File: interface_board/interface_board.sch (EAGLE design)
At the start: 101 parts, among them IC1 V7805-1000, IC6 LAN9512-JZX, K1 61400416021, Q6 CTS_32X25_SMD, U1 SFW15R-1STE1LF, U2 SFW15R-1STE1LF, U3 DMG1012T, U5 PAM2306DYPAA

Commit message: picam360
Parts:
- removed C11: UUD1A220MCL1GS(22u), resistor:CPOL-EU153CLV-0405
- removed C15: UUD1E100MCL1GS(10u), resistor:CPOL-EU153CLV-0405
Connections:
- removed net 3V3A1: C32.2, C33.2, C34.2, C35.2, C36.2, C37.2, C38.2, FB2.P$1, IC6.VDD33A@1, IC6.VDD33A@2, IC6.VDD33A@3, IC6.VDD33A@4, IC6.VDD33A@5, IC6.VDD33A@6, IC6.VDD33A@7
- removed net N$47: IC6.USBDM2, JP5.D-
- removed net N$48: IC6.USBDP2, JP5.D+
- removed net USBD3_N: IC6.USBDM3, K1.D-
- removed net USBD3_P: IC6.USBDP3, K1.D+
- new net USB3_N: IC6.USBDM3, JP5.D-
- new net USB3_P: IC6.USBDP3, JP5.D+
- new net USBD2_N: IC6.USBDM2, K1.D-
- new net USBD2_P: IC6.USBDP2, K1.D+
- net +5V: no longer C11.+
- net 3V3A: now also C32.2, C33.2, C34.2, C35.2, C36.2, C37.2, C38.2, FB2.P$1, IC6.VDD33A@1, IC6.VDD33A@2, IC6.VDD33A@3, IC6.VDD33A@4, IC6.VDD33A@5, IC6.VDD33A@6, IC6.VDD33A@7
- net GND: no longer C11.-, C15.-
- net N$39: no longer C15.+

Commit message: interface board
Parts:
- removed C16: 1u, resistor:C-EUC0402
- removed C17: 10n, resistor:C-EUC0402
- removed F1: MF-MSMF200-2, openblw:MF-MSMF075/24
- removed FB1, FB4: HR2220V801R-10, resistor:L-EUL5650M
- removed IC1: V7805-1000, openblw:VR_1OUTXX
- removed JP2, JP3: M20-9980346, pinhead:PINHD-2X3
- removed JP4: M20-9990246, openblw:PINHD-1X2
- removed L3: SRP1245A-100M, openblw:SRP1250A
- removed R18: 1K, resistor:R-EU_R0402
- removed U$1: 282836-2, openblw:282836-2
- removed U$2: M20-9980346, openblw:282836-2
- JP1: device pinhead:PINHD-2X4 -> pinhead:PINHD-2X20
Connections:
- removed net +12V: C16.1, F1.1, L3.2, U$2.CON01
- removed net AGND: FB4.1, JP2.5, JP2.6, U$1.CON01
- removed net AVCC: FB1.1, JP2.1, JP2.2, U$1.CON02
- removed net N$38: C17.1, R18.2
- removed net N$39: F1.2, IC1.IN
- removed net N$6: FB1.2, L3.1, R18.1
- net +3V3: no longer JP3.5, JP3.6, JP4.1
- net +5V: no longer IC1.OUT
- net GND: now also JP1.13, JP1.14; no longer C16.2, C17.2, FB4.2, IC1.GND, JP3.1, JP4.2, U$2.CON02

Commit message: refactoring
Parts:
- removed C12, C13, C14: 47u, resistor:C-EUC1206
- removed C4, C5: 100p, resistor:C-EUC0402
- removed C6, C7: 10u, resistor:C-EUC0805
- removed L1, L2: SRN4018-4R7M(4.7u), openblw:BOURNS-SRN4018
- removed PCB1: 1473005-4, openblw:RPI_COMPUTE
- removed R11, R12, R4, R5: 100K, resistor:R-EU_R0402
- removed R13, R14, R16, R17: 1.8K, resistor:R-EU_R0402
- removed R15, R6: 470R, resistor:R-EU_R0402
- removed R7, R8, R9: 0R, resistor:R-EU_R0805
- removed U3: DMG1012T, openblw:DMG1012T
- removed U5: PAM2306DYPAA, openblw:PAM2306
- added C16: 1u, resistor:C-EUC0402
- added C17: 10n, resistor:C-EUC0402
- added FB1, FB4: HR2220V801R-10, resistor:L-EUL5650M
- added IC1: V7805-1000, openblw:VR_1OUTXX
- added JP2, JP3: M20-9980346, pinhead+:PINHD-2X3SMT
- added JP4: (no value), pinhead:PINHD-1X3
- added L3: SRP1245A-100M, openblw:SRP1250A
- added Q1: IRLML6346TRPBF, openblw:NMOS-FETSOT23
- added R18: 1K, resistor:R-EU_R0402
- added U$2, U$4, U$7, U$8: 282836-2, openblw:282836-2
- C10, C41, C42: device rcl:C-EUC0805 -> resistor:C-EUC0402
- C2: value 10u -> UWT1E221MNL1GS(220u); device resistor:C-EUC0805 -> resistor:CPOL-EU153CLV-0810
- C21, C22, C23, C24, C26, C27, C28, C29, C30, C31, C32, C33, C34, C35, C36, C37, C38, C39, C40, C43, C44, C45, C8, C9: device rcl:C-EUC0603 -> resistor:C-EUC0402
- C3: value 10u -> 1uF; device resistor:C-EUC0805 -> SparkFun-Capacitors:CAP0603-CAP
- JP1: value M20-9980446 -> M20-9990446; device pinhead:PINHD-2X20 -> pinhead:PINHD-2X5
- JP5: value USB-IDMICRO -> (none); device openblw:USB-IDMICRO -> pinhead:PINHD-1X3
- LED1: value RED -> LTW-5630AZL50; device led:LEDCHIP-LED0603 -> openblw:LTW-5630AZL
- LED2: value GREEN -> LTW-5630AZL50; device led:LEDCHIP-LED0603 -> openblw:LTW-5630AZL
- R1: value 100K -> 4.99K
- R10, R19, R20, R25, R26, R27, R28, R29, R30, R31, R32, R33: device rcl:R-EU_R0603 -> resistor:R-EU_R0402
- R2: value 450K -> 100K
- R3: value 200K -> 1K
- U1: value SFW15R-1STE1LF -> AL5812MP-13; device openblw:RPI_CAMERA -> openblw:AL5812MP-13
- U2: value SFW15R-1STE1LF -> MPU-9250; device openblw:RPI_CAMERA -> invensense:MPU-9250
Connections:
- removed net +1V8: C5.1, C7.1, L2.1, R3.1, R9.2
- removed net BOTTOM_LIGHT_ENABLED: PCB1.59/GPIO17
- removed net CAM0_C_N: PCB1.144/CAM0_CN*, U1.CAM_CK_N@8
- removed net CAM0_C_P: PCB1.142/CAM0_CP*, U1.CAM_CK_P@9
- removed net CAM0_D0_N: PCB1.138/CAM0_DN0*, U1.CAM_D0_N@2
- removed net CAM0_D0_P: PCB1.136/CAM0_DP0*, U1.CAM_D0_P@3
- removed net CAM0_D1_N: PCB1.150/CAM0_DN1*, U1.CAM_D1_N@5
- removed net CAM0_D1_P: PCB1.148/CAM0_DP1*, U1.CAM_D1_P@6
- removed net CAM0_IO0: PCB1.36/GPIO31, U1.CAM_IO0@11
- removed net CAM0_IO1: PCB1.34/GPIO30, U1.CAM_IO1@12
- removed net CAM0_SCL: PCB1.30/GPIO29, R13.1, U1.CAM_SCL@13
- removed net CAM0_SDA: PCB1.28/GPIO28, R14.1, U1.CAM_SDA@14
- removed net CAM1_C_N: PCB1.149/CAM1_CN*, U2.CAM_CK_N@8
- removed net CAM1_C_P: PCB1.147/CAM1_CP*, U2.CAM_CK_P@9
- removed net CAM1_D0_N: PCB1.161/CAM1_DN0*, U2.CAM_D0_N@2
- removed net CAM1_D0_P: PCB1.159/CAM1_DP0*, U2.CAM_D0_P@3
- removed net CAM1_D1_N: PCB1.155/CAM1_DN1*, U2.CAM_D1_N@5
- removed net CAM1_D1_P: PCB1.153/CAM1_DP1*, U2.CAM_D1_P@6
- removed net CAM1_IO0: PCB1.11/GPIO3, U2.CAM_IO0@11
- removed net CAM1_IO1: PCB1.9/GPIO2, U2.CAM_IO1@12
- removed net CAM1_SCL: PCB1.5/GPIO1, R17.1, U2.CAM_SCL@13
- removed net CAM1_SDA: PCB1.3/GPIO0, R16.1, U2.CAM_SDA@14
- removed net CM_1V8: C12.1, PCB1.183/1V8, PCB1.184/1V8, PCB1.185/1V8, PCB1.186/1V8, R9.1
- removed net CM_3V3: C13.1, PCB1.189/VDAC, PCB1.190/VDAC, PCB1.191/3V3, PCB1.192/3V3, PCB1.193/3V3, PCB1.194/3V3, R8.1
- removed net CM_VBAT: C14.1, PCB1.197/VBAT, PCB1.198/VBAT, PCB1.199/VBAT, PCB1.200/VBAT, R7.1
- removed net EMMC_DISABLE_N: PCB1.2/EMMC_DISABLE_N
- removed net EXT0/UART1_TX: JP1.6, PCB1.70/GPIO40
- removed net EXT1/UART1_RX: JP1.4, PCB1.72/GPIO41
- removed net GPIO47_1V8: PCB1.90/GPIO47_1V8, U3.G
- removed net N$10: C5.2, R3.2, R4.1, U5.FB2@10
- removed net N$11: PCB1.154/NC
- removed net N$12: PCB1.156/NC
- removed net N$13: PCB1.158/NC
- removed net N$14: PCB1.160/NC
- removed net N$15: PCB1.162/NC
- removed net N$16: PCB1.10/NC
- removed net N$17: PCB1.12/NC
- removed net N$18: PCB1.14/NC
- removed net N$19: PCB1.16/NC
- removed net N$2: L1.2, U5.LX1@8
- removed net N$20: PCB1.18/NC
- removed net N$21: PCB1.20/NC
- removed net N$22: PCB1.22/NC
- removed net N$23: PCB1.24/NC
- removed net N$24: PCB1.124/NC
- removed net N$25: PCB1.126/NC
- removed net N$26: PCB1.128/NC
- removed net N$27: PCB1.130/NC
- removed net N$28: PCB1.132/NC
- removed net N$29: PCB1.4/NC
- removed net N$30: PCB1.6/NC
- removed net N$31: PCB1.82/GPIO44, R12.1
- removed net N$32: LED2.A, R15.2
- removed net N$33: LED2.C, U3.D
- removed net N$34: PCB1.84/GPIO45, R11.1
- removed net N$35: PCB1.8/NC
- removed net N$8: C4.2, R2.2, R5.1, U5.FB1@4
- removed net TOP_LIGHT_ENABLED: PCB1.57/GPIO16
- removed net UART0_RX: JP1.5, PCB1.53/GPIO15
- removed net UART0_TX: JP1.3, PCB1.51/GPIO14
- removed net USB3_N: IC6.USBDM3, JP5.D-
- removed net USB3_P: IC6.USBDP3, JP5.D+
- new net +12V: C1.2, C16.1, C2.+, IC1.IN, L3.2, LED1.A, U$4.CON02, U1.VCC
- new net AGND: FB4.1, JP2.5, JP2.6, U$2.CON02
- new net AIN1: JP1.6
- new net AIN2: JP1.5
- new net AOUT1: U$8.CON01
- new net AOUT2: U$8.CON02
- new net AVCC: FB1.1, JP2.1, JP2.2, U$2.CON01
- new net BIN1: JP1.7
- new net BIN2: JP1.8
- new net BOUT1: U$7.CON02
- new net BOUT2: U$7.CON01
- new net LIGHT_PWM: JP1.1, R3.2
- new net N$38: C17.1, R18.2
- new net N$5: R1.2, U1.RSET
- new net N$6: Q1.D, R1.1
- new net PWMA: JP1.4
- new net PWMB: JP1.9
- new net TWI_SCL: U2.SCL/SCLK
- new net TWI_SDA: U2.SDA/SDI
- new net VCC: U2.NCS, U2.RESV, U2.VDD, U2.VDDIO
- net +3V3: now also JP1.2, JP3.5, JP3.6; no longer C4.1, C6.1, L1.1, PCB1.39/GPIO0-27_VREF, PCB1.40/GPIO0-27_VREF, PCB1.41/GPIO28-45_VREF, PCB1.42/GPIO28-45_VREF, R13.2, R14.2, R15.1, R16.2, R17.2, R2.1, R6.1, R7.2, R8.2, U1.CAM_3V3@15, U2.CAM_3V3@15
- net +5V: now also IC1.OUT; no longer C2.1, C3.1, JP1.1, JP1.2, JP5.VBUS, R1.1, U5.EN1@6, U5.VIN1@7, U5.VIN2@1
- net GND: now also C1.1, C16.2, C17.2, C2.-, C3.1, FB4.2, IC1.GND, JP1.10, JP1.3, JP3.1, Q1.S, R2.1, U$4.CON01, U1.EP, U1.GND, U2.ADO/SDO, U2.FSYNC, U2.GND, U2.RESV2; no longer C1.2, C12.2, C13.2, C14.2, C2.2, C3.2, C6.2, C7.2, JP1.13, JP1.14, JP1.7, JP1.8, JP5.GND, LED1.C, PCB1.1/GND, PCB1.103/GND, PCB1.104/GND, PCB1.109/GND, PCB1.110/GND, PCB1.115/GND, PCB1.121/GND, PCB1.122/GND, PCB1.127/GND, PCB1.13/GND, PCB1.133/GND, PCB1.134/GND, PCB1.139/GND, PCB1.140/GND, PCB1.145/GND, PCB1.146/GND, PCB1.151/GND, PCB1.152/GND, PCB1.157/GND, PCB1.163/GND, PCB1.164/GND, PCB1.168/USB_OTGID, PCB1.169/GND, PCB1.170/GND, PCB1.181/GND, PCB1.182/GND, PCB1.187/GND, PCB1.188/GND, PCB1.19/GND, PCB1.195/GND, PCB1.196/GND, PCB1.25/GND, PCB1.26/GND, PCB1.31/GND, PCB1.32/GND, PCB1.37/GND, PCB1.38/GND, PCB1.43/GND, PCB1.44/GND, PCB1.49/GND, PCB1.50/GND, PCB1.55/GND, PCB1.56/GND, PCB1.61/GND, PCB1.62/GND, PCB1.67/GND, PCB1.68/GND, PCB1.7/GND, PCB1.73/GND, PCB1.74/GND, PCB1.79/GND, PCB1.80/GND, PCB1.85/GND, PCB1.86/GND, PCB1.91/GND, PCB1.92/GND, PCB1.97/GND, PCB1.98/GND, R11.2, R12.2, R4.2, R5.2, U1.CAM_GND@1, U1.CAM_GND@10, U1.CAM_GND@4, U1.CAM_GND@7, U2.CAM_GND@1, U2.CAM_GND@10, U2.CAM_GND@4, U2.CAM_GND@7, U3.S, U5.GND@3, U5.GND@9, U5.PAD
- net LAN_RUN: no longer PCB1.21/GPIO6
- net N$1: now also LED1.C, LED2.A; no longer C1.1, R1.2, U5.EN2@12
- net N$3: now also FB1.2, L3.1, R18.1; no longer U5.NC1@5
- net N$4: now also C3.2, U2.REGOUT; no longer U5.NC2@11
- net N$7: now also Q1.G, R2.2, R3.1; no longer L2.2, U5.LX2@2
- net N$9: now also LED2.C, U1.LED; no longer LED1.A, R6.2
- net USB_D_N: no longer PCB1.167/USB_DM**
- net USB_D_P: no longer PCB1.165/USB_DP**
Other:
- note removed: "Camera"
- note removed: "Interfaces"
- note removed: "Power"
- note removed: "RPCM"

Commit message: refactoring
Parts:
- removed JP5: (no value), pinhead:PINHD-1X3
- added JP6: USB-IDMICRO, openblw:USB-IDMICRO
- JP2, JP3: device pinhead+:PINHD-2X3SMT -> pinhead:PINHD-2X3
- JP4: device pinhead:PINHD-1X3 -> pinhead:PINHD-2X3
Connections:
- net +5V: now also JP6.VBUS
- net GND: now also JP6.GND
- net USB_D_N: now also JP6.D-
- net USB_D_P: now also JP6.D+
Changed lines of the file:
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@@
 <part name="L3" library="openblw" deviceset="SRP1250A" device="" value="SRP1245A-100M"/>
 <part name="FB4" library="resistor" deviceset="L-EU" device="L5650M" value="HR2220V801R-10"/>
-<part name="JP2" library="pinhead+" deviceset="PINHD-2X3" device="SMT" value="M20-9980346"/>
-<part name="JP3" library="pinhead+" deviceset="PINHD-2X3" device="SMT" value="M20-9980346"/>
+<part name="JP2" library="pinhead" deviceset="PINHD-2X3" device="" value="M20-9980346"/>
+<part name="JP3" library="pinhead" deviceset="PINHD-2X3" device="" value="M20-9980346"/>
 <part name="V7" library="supply" deviceset="+3V3" device=""/>
 <part name="GND11" library="supply" deviceset="GND" device=""/>
@@
 <part name="Q6" library="raspi" deviceset="CTS_32X25_SMD" device=""/>
 <part name="GND53" library="supply1" deviceset="GND" device=""/>
-<part name="JP4" library="pinhead" deviceset="PINHD-1X3" device=""/>
-<part name="JP5" library="pinhead" deviceset="PINHD-1X3" device=""/>
 <part name="U2" library="invensense" deviceset="MPU-9250" device=""/>
 <part name="GND6" library="SparkFun-Aesthetics" deviceset="GND" device=""/>
 <part name="SUPPLY1" library="SparkFun-Aesthetics" deviceset="VCC" device=""/>
 <part name="C3" library="SparkFun-Capacitors" deviceset="CAP" device="0603-CAP" value="1uF"/>
+<part name="JP6" library="openblw" deviceset="USB-ID" device="MICRO"/>
+<part name="GND8" library="supply1" deviceset="GND" device=""/>
+<part name="P+1" library="supply1" deviceset="+5V" device=""/>
+<part name="JP4" library="pinhead" deviceset="PINHD-2X3" device=""/>
 </parts>
 <sheets>
@@
 <instance part="GND13" gate="1" x="332.74" y="137.16"/>
 <instance part="GND15" gate="1" x="304.8" y="137.16"/>
-<instance part="JP4" gate="A" x="116.84" y="142.24" rot="R180"/>
-<instance part="JP5" gate="A" x="116.84" y="132.08" rot="R180"/>
 <instance part="U2" gate="G$1" x="195.58" y="132.08"/>
 <instance part="GND6" gate="1" x="231.14" y="96.52"/>
 <instance part="SUPPLY1" gate="G$1" x="165.1" y="170.18"/>
 <instance part="C3" gate="G$1" x="167.64" y="124.46" rot="R90"/>
+<instance part="JP4" gate="A" x="101.6" y="129.54"/>
 </instances>
 <busses>
@@
 <instance part="Q6" gate="G$2" x="177.8" y="73.66" rot="R90"/>
 <instance part="GND53" gate="1" x="160.02" y="78.74" rot="R270"/>
+<instance part="JP6" gate="G$1" x="157.48" y="114.3" rot="R270"/>
+<instance part="GND8" gate="1" x="142.24" y="114.3"/>
+<instance part="P+1" gate="1" x="177.8" y="119.38" rot="R270"/>
 </instances>
 <busses>
@@
 <pinref part="GND53" gate="1" pin="GND"/>
 <junction x="162.56" y="78.74"/>
+</segment>
+<segment>
+<pinref part="JP6" gate="G$1" pin="GND"/>
+<wire x1="157.48" y1="116.84" x2="157.48" y2="119.38" width="0.1524" layer="91"/>
+<pinref part="GND8" gate="1" pin="GND"/>
+<wire x1="157.48" y1="119.38" x2="142.24" y2="119.38" width="0.1524" layer="91"/>
+<wire x1="142.24" y1="119.38" x2="142.24" y2="116.84" width="0.1524" layer="91"/>
 </segment>
 </net>
@@
 <pinref part="K1" gate="G$1" pin="VCC"/>
 </segment>
+<segment>
+<pinref part="JP6" gate="G$1" pin="VBUS"/>
+<wire x1="160.02" y1="116.84" x2="160.02" y2="119.38" width="0.1524" layer="91"/>
+<pinref part="P+1" gate="1" pin="+5V"/>
+<wire x1="160.02" y1="119.38" x2="175.26" y2="119.38" width="0.1524" layer="91"/>
+</segment>
 </net>
 <net name="USBD2_N" class="3">
@@
 <segment>
 <pinref part="IC6" gate="G$1" pin="USBDM0"/>
-<wire x1="238.76" y1="127" x2="177.8" y2="127" width="0.1524" layer="91"/>
-<label x="177.8" y="127" size="1.778" layer="95" rot="R180" xref="yes"/>
+<wire x1="238.76" y1="127" x2="162.56" y2="127" width="0.1524" layer="91"/>
+<label x="152.4" y="127" size="1.778" layer="95" rot="R180" xref="yes"/>
+<pinref part="JP6" gate="G$1" pin="D-"/>
+<wire x1="162.56" y1="127" x2="152.4" y2="127" width="0.1524" layer="91"/>
+<wire x1="162.56" y1="116.84" x2="162.56" y2="127" width="0.1524" layer="91"/>
+<junction x="162.56" y="127"/>
 </segment>
 </net>
@@
 <segment>
 <pinref part="IC6" gate="G$1" pin="USBDP0"/>
-<wire x1="238.76" y1="124.46" x2="177.8" y2="124.46" width="0.1524" layer="91"/>
-<label x="177.8" y="124.46" size="1.778" layer="95" rot="R180" xref="yes"/>
-</segment>
-</net>
+<wire x1="238.76" y1="124.46" x2="165.1" y2="124.46" width="0.1524" layer="91"/>
+<label x="152.4" y="124.46" size="1.778" layer="95" rot="R180" xref="yes"/>
+<pinref part="JP6" gate="G$1" pin="D+"/>
+<wire x1="165.1" y1="124.46" x2="152.4" y2="124.46" width="0.1524" layer="91"/>
+<wire x1="165.1" y1="116.84" x2="165.1" y2="124.46" width="0.1524" layer="91"/>
+<junction x="165.1" y="124.46"/>
+</segment>
+</net>

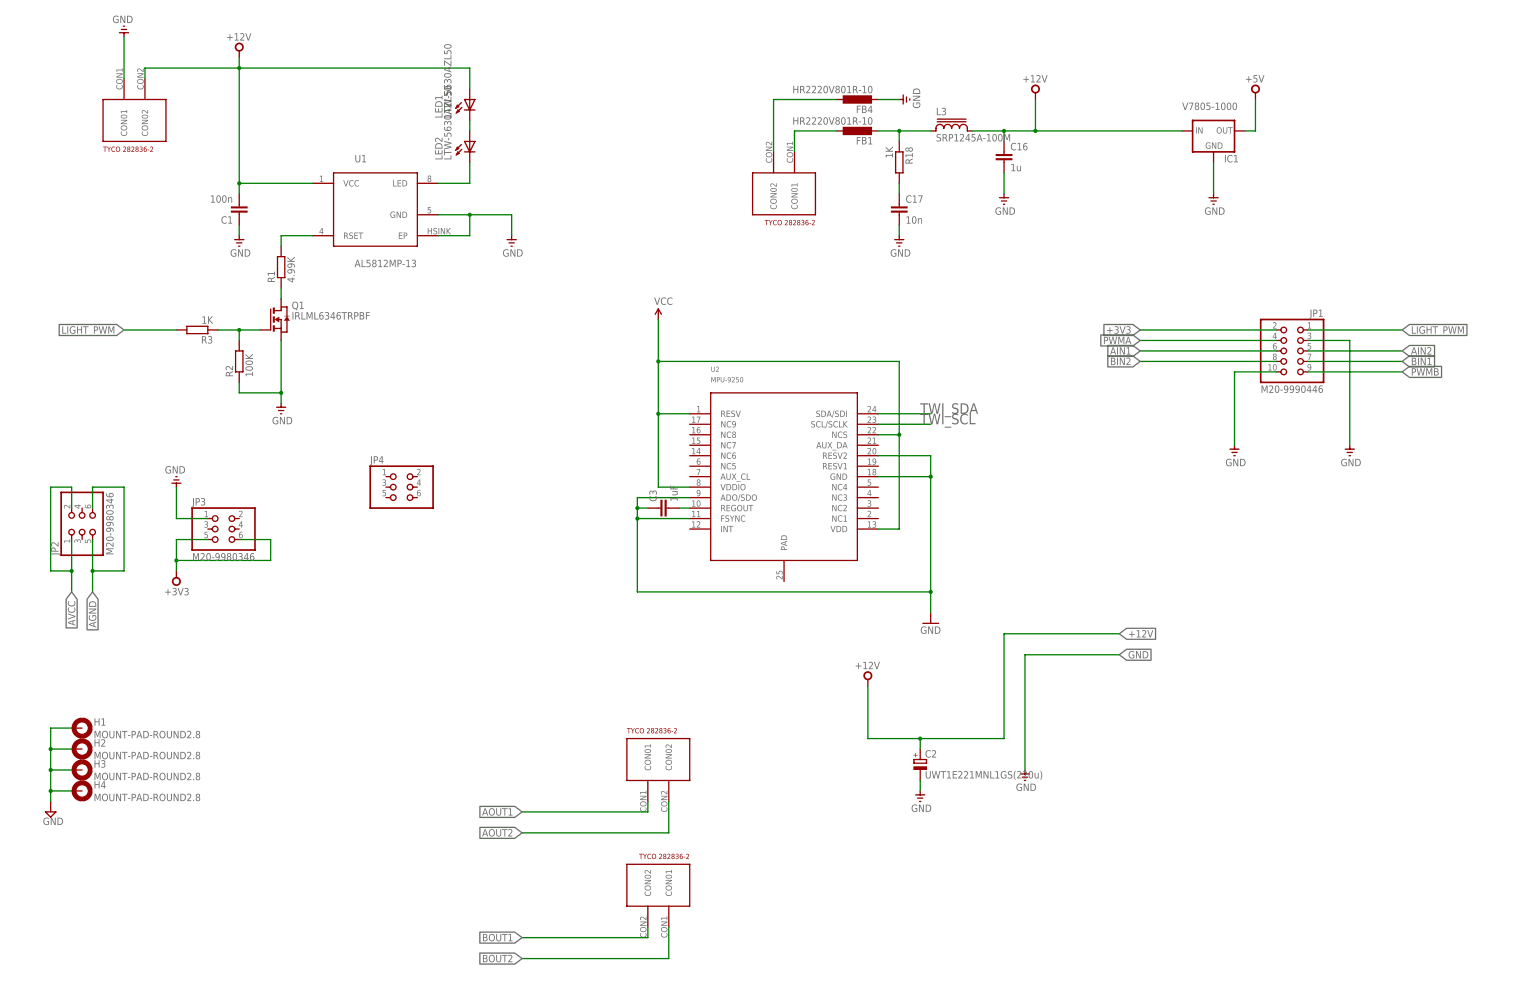
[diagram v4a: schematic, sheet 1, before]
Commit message: interface_board provisional wiring
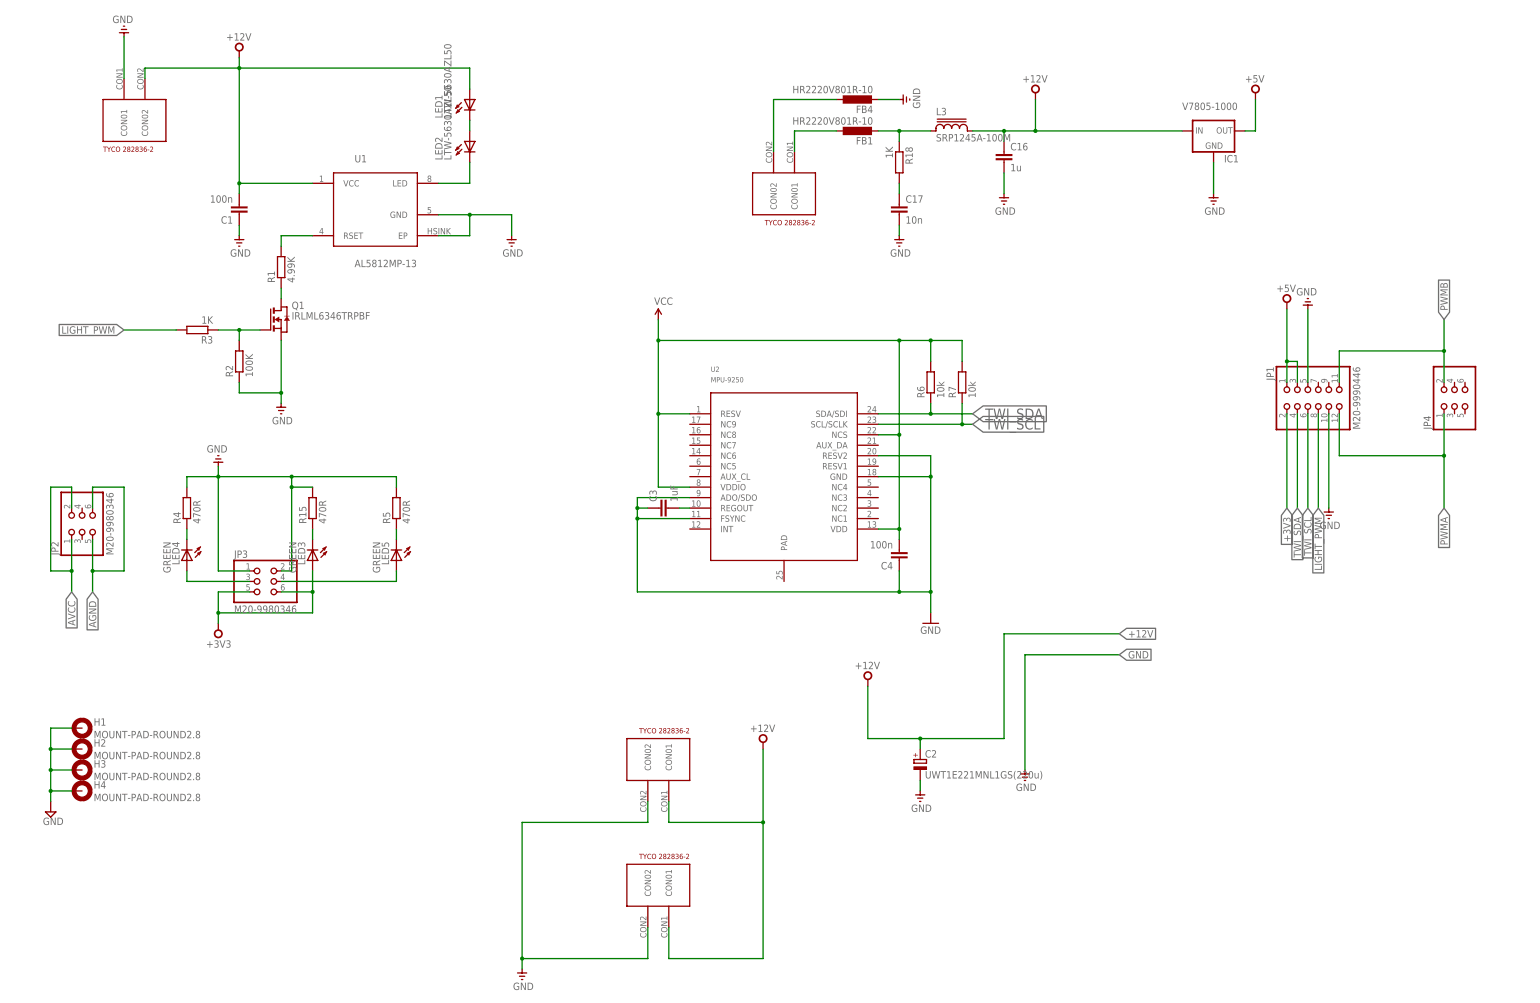
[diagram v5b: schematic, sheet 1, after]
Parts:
- added C4: 100n, resistor:C-EUC0402
- added LED3, LED4, LED5: GREEN, led:LEDCHIP-LED0603
- added R15, R4, R5: 470R, resistor:R-EU_R0402
- added R6, R7: 10k, resistor:R-EU_R0402
- C10, C41, C42: device resistor:C-EUC0402 -> resistor:C-EUC0603
- JP1: device pinhead:PINHD-2X5 -> pinhead:PINHD-2X6
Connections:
- removed net AIN1: JP1.6
- removed net AIN2: JP1.5
- removed net AOUT1: U$8.CON01
- removed net AOUT2: U$8.CON02
- removed net BIN1: JP1.7
- removed net BIN2: JP1.8
- removed net BOUT1: U$7.CON02
- removed net BOUT2: U$7.CON01
- new net N$11: JP3.4, LED5.A
- new net N$12: LED5.C, R5.1
- new net N$14: LED3.C, R15.1
- new net N$2: LED4.C, R4.1
- new net N$8: JP3.3, LED4.A
- net +12V: now also U$7.CON01, U$8.CON01
- net +3V3: now also LED3.A
- net +5V: now also JP1.1, JP1.3
- net GND: now also C4.1, JP1.5, JP3.2, R15.2, R4.2, R5.2, U$7.CON02, U$8.CON02; no longer JP1.3
- net LIGHT_PWM: now also JP1.8; no longer JP1.1
- net PWMA: now also JP1.12, JP4.1; no longer JP1.4
- net PWMB: now also JP1.11, JP4.2; no longer JP1.9
- net TWI_SCL: now also JP1.6, R7.1
- net TWI_SDA: now also JP1.4, R6.1
- net VCC: now also C4.2, R6.2, R7.2
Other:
- moved on the sheet: JP3, JP4

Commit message: for 2017 version
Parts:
- removed K1: 61400416021, openblw:61400416021
- added K2: 61400826021, Wuerth_Elektronik_eiCan_Communication_Connectors_v2.2:61400826021
- added R8: 0, resistor:R-EU_R0402
- added R9: 10k, resistor:R-EU_R0402
- JP1: device pinhead:PINHD-2X6 -> pinhead:PINHD-2X8
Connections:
- removed net VCC: C4.2, R6.2, R7.2, U2.NCS, U2.RESV, U2.VDD, U2.VDDIO
- new net N$10: JP1.14, R8.2
- new net USBD3_N: IC6.USBDM3, K2.D-@2
- new net USBD3_P: IC6.USBDP3, K2.D+@2
- net +3V3: now also C4.2, R6.2, R7.2, R9.2, U2.NCS, U2.RESV, U2.VDD, U2.VDDIO
- net +5V: now also K2.VCC@1, K2.VCC@2; no longer K1.VCC
- net GND: now also JP1.13, K2.GND@1, K2.GND@2; no longer K1.GND
- net LAN_RUN: now also R8.1, R9.1
- net USBD2_N: now also K2.D-@1; no longer K1.D-
- net USBD2_P: now also K2.D+@1; no longer K1.D+
